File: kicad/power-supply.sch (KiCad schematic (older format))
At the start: 26 parts, among them Q2 2N7002, Q3 MMBT3904, Q4 MMBT3904, Q5 ZXMP10A13FTA, SW6 Ein/Aus, X4 GND-Öse

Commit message: BOM aktualisiert, Zenerdiode: Pinout IPC-konform gestaltet, ...
siehe https://gitlab.com/kicad/libraries/kicad-symbols/-/issues/3157
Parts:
- C22: Index (none) -> 37
- C23: Index (none) -> 44
- C24: Index (none) -> 7
- D8: Index (none) -> 32
- D9: footprint Diode_SMD:D_SOT-23_ANK -> Package_TO_SOT_SMD:SOT-23; symbol Diode:BZX84Cxx -> htl_semiconductors:BZX84Cxx; Index (none) -> 3
- F1, Item3: Index (none) -> 23
- Item4: Index (none) -> 18
- Q2: Index (none) -> 20
- Q3, Q4: Index (none) -> 36
- Q5: Index (none) -> 8
- R32, R33, R34, R37: Index (none) -> 15
- R35: Index (none) -> 26
- R36, R38, R40: Index (none) -> 12
- R39: DistOrderNr (none) -> R3216-22k; Distributor LCSC -> AufLager; Index (none) -> 57
- R41, R42, R43: Index (none) -> 4
- SW6: Index (none) -> 33
- X4: DistOrderNr (none) -> C238129; Distributor (none) -> LCSC; Index (none) -> 27
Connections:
- net GNDPWR: now also D9.1 (A); no longer D9.2 (A)
- net at Q2.1 (G), Q3.1 (B), R33.1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: now also D9.3 (K); no longer D9.1 (K)
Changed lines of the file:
@@
 F 10 "500" H 2700 3650 50  0001 C CNN "PriceForQty"
 F 11 "https://lcsc.com/product-detail/Tactile-Switches_XKB-Connectivity-TS-1187A-B-A-B_C318884.html" H 2700 3650 50  0001 C CNN "Weblink"
+F 12 "33" H 2700 3650 50  0001 C CNN "Index"
 	1    2700 3650
 	0    -1   -1   0
@@
 F 6 "LCSC" H 2700 4550 50  0001 C CNN "Distributor"
 F 7 "10kΩ ±5% 0.25W ±100ppm/℃ 3216 Chip Resistor" H 2700 4550 50  0001 C CNN "Notes"
+F 8 "15" H 2700 4550 50  0001 C CNN "Index"
 	1    2700 4550
 	1    0    0    -1
@@
 F 6 "LCSC" H 2350 5200 50  0001 C CNN "Distributor"
 F 7 "10kΩ ±5% 0.25W ±100ppm/℃ 3216 Chip Resistor" H 2350 5200 50  0001 C CNN "Notes"
+F 8 "15" H 2350 5200 50  0001 C CNN "Index"
 	1    2350 5200
 	1    0    0    -1
 $EndComp
 $Comp
-L Diode:BZX84Cxx D9
+L htl_semiconductors:BZX84Cxx D9
 U 1 1 60911C30
 P 2700 5200
 F 0 "D9" V 2654 5279 50  0000 L CNN
 F 1 "4V7" V 2745 5279 50  0000 L CNN
-F 2 "Diode_SMD:D_SOT-23_ANK" H 2700 5025 50  0001 C CNN
+F 2 "Package_TO_SOT_SMD:SOT-23" H 2700 5025 50  0001 C CNN
 F 3 "https://diotec.com/tl_files/diotec/files/pdf/datasheets/bzx84c2v4.pdf" H 2700 5200 50  0001 C CNN
 F 4 "C12727" H 2700 5200 50  0001 C CNN "DistOrderNr"
@@
 F 7 "0.014" H 2700 5200 50  0001 C CNN "PriceEUR"
 F 8 "50" H 2700 5200 50  0001 C CNN "PriceForQty"
+F 9 "3" H 2700 5200 50  0001 C CNN "Index"
 	1    2700 5200
 	0    1    1    0
@@
 F 7 "50" H 3300 4850 50  0001 C CNN "PriceForQty"
 F 8 "https://lcsc.com/product-detail/Transistors-NPN-PNP_KEXIN-MMBT3904_C382281.html" H 3300 4850 50  0001 C CNN "Weblink"
+F 9 "36" H 3300 4850 50  0001 C CNN "Index"
 	1    3300 4850
 	1    0    0    -1
@@
 F 7 "50" H 4050 4850 50  0001 C CNN "PriceForQty"
 F 8 "https://lcsc.com/product-detail/Transistors-NPN-PNP_KEXIN-MMBT3904_C382281.html" H 4050 4850 50  0001 C CNN "Weblink"
+F 9 "36" H 4050 4850 50  0001 C CNN "Index"
 	1    4050 4850
 	-1   0    0    -1
@@
 F 6 "LCSC" H 3650 3400 50  0001 C CNN "Distributor"
 F 7 "10kΩ ±5% 0.25W ±100ppm/℃ 3216 Chip Resistor" H 3650 3400 50  0001 C CNN "Notes"
+F 8 "15" H 3650 3400 50  0001 C CNN "Index"
 	1    3650 3400
 	1    0    0    -1
@@
 F 5 "C229599" H 3250 5400 50  0001 C CNN "DistOrderNr"
 F 6 "LCSC" H 3250 5400 50  0001 C CNN "Distributor"
+F 7 "26" H 3250 5400 50  0001 C CNN "Index"
 	1    3250 5400
 	1    0    0    -1
@@
 F 9 "0.0106" H 4050 3400 50  0001 C CNN "PriceEUR"
 F 10 "500" H 4050 3400 50  0001 C CNN "PriceForQty"
+F 11 "44" H 4050 3400 50  0001 C CNN "Index"
 	1    4050 3400
 	1    0    0    -1
@@
 F 9 "1kΩ ±5% 0.25W ±100ppm/℃ 1206 Chip Resistor" H 4500 5300 50  0001 C CNN "Notes"
 F 10 "50" H 4500 5300 50  0001 C CNN "PriceForQty"
+F 11 "12" H 4500 5300 50  0001 C CNN "Index"
 	1    4500 5300
 	1    0    0    -1
@@
 F 10 "200" H 1700 1500 50  0001 C CNN "PriceForQty"
 F 11 "https://lcsc.com/product-detail/Fuse-Holders_Shenzhen-lanson-Elec-LS-502_C182320.html" H 1700 1500 50  0001 C CNN "Weblink"
+F 12 "23" H 1700 1500 50  0001 C CNN "Index"
 	1    1700 1500
 	0    1    1    0
@@
 F 8 "https://lcsc.com/product-detail/TVS_Brightking-Elec-TAIWAN-SMCJ48A_C310056.html" H 2000 1700 50  0001 C CNN "Weblink"
 F 9 "TVS-Diode, 1500W, 77.4V, 19.4A" H 2000 1700 50  0001 C CNN "Notes"
+F 10 "32" H 2000 1700 50  0001 C CNN "Index"
 	1    2000 1700
 	0    1    1    0
@@
 F 10 "100" H 1700 1150 50  0001 C CNN "PriceForQty"
 F 11 "https://lcsc.com/product-detail/Cartridge-Fuses_Littelfuse-0618010-MXP_C142673.html" H 1700 1150 50  0001 C CNN "Weblink"
+F 12 "18" H 1700 1150 50  0001 C CNN "Index"
 	1    1700 1150
 	-1   0    0    1
@@
 F 9 "0.2191" H 5000 3700 50  0001 C CNN "PriceEUR"
 F 10 "100" H 5000 3700 50  0001 C CNN "PriceForQty"
+F 11 "8" H 5000 3700 50  0001 C CNN "Index"
 	1    5000 3700
 	1    0    0    1
@@
 F 10 "50" H 1800 5250 50  0001 C CNN "PriceForQty"
 F 11 "https://lcsc.com/product-detail/MOSFET_Guangdong-Hottech-2N7002_C181082.html" H 1800 5250 50  0001 C CNN "Weblink"
+F 12 "20" H 1800 5250 50  0001 C CNN "Index"
 	1    1800 5250
 	-1   0    0    -1
@@
 F 5 "C17928" H 7550 4500 50  0001 C CNN "DistOrderNr"
 F 6 "LCSC" H 7550 4500 50  0001 C CNN "Distributor"
+F 7 "4" H 7550 4500 50  0001 C CNN "Index"
 	1    7550 4500
 	0    1    1    0
@@
 F 5 "C17928" H 9550 4500 50  0001 C CNN "DistOrderNr"
 F 6 "LCSC" H 9550 4500 50  0001 C CNN "Distributor"
+F 7 "4" H 9550 4500 50  0001 C CNN "Index"
 	1    9550 4500
 	0    1    1    0
@@
 F 3 "~" H 5100 5400 50  0001 C CNN
 F 4 "0.01" H 5100 5400 50  0001 C CNN "PriceEUR"
-F 5 "LCSC" H 5100 5400 50  0001 C CNN "Distributor"
+F 5 "AufLager" H 5100 5400 50  0001 C CNN "Distributor"
+F 6 "R3216-22k" H 5100 5400 50  0001 C CNN "DistOrderNr"
+F 7 "57" H 5100 5400 50  0001 C CNN "Index"
 	1    5100 5400
 	1    0    0    -1
@@
 F 9 "1kΩ ±5% 0.25W ±100ppm/℃ 1206 Chip Resistor" H 5100 5850 50  0001 C CNN "Notes"
 F 10 "50" H 5100 5850 50  0001 C CNN "PriceForQty"
+F 11 "12" H 5100 5850 50  0001 C CNN "Index"
 	1    5100 5850
 	1    0    0    -1
@@
 F 9 "0.0233" H 5600 5950 50  0001 C CNN "PriceEUR"
 F 10 "100" H 5600 5950 50  0001 C CNN "PriceForQty"
+F 11 "7" H 5600 5950 50  0001 C CNN "Index"
 	1    5600 5950
 	1    0    0    -1
@@
 F 6 "LCSC" H 1700 4550 50  0001 C CNN "Distributor"
 F 7 "10kΩ ±5% 0.25W ±100ppm/℃ 3216 Chip Resistor" H 1700 4550 50  0001 C CNN "Notes"
+F 8 "15" H 1700 4550 50  0001 C CNN "Index"
 	1    1700 4550
 	1    0    0    -1
@@
 F 9 "0.0123" H 2850 3400 50  0001 C CNN "PriceEUR"
 F 10 "50" H 2850 3400 50  0001 C CNN "PriceForQty"
+F 11 "37" H 2850 3400 50  0001 C CNN "Index"
 	1    2850 3400
 	0    -1   -1   0
@@
 F 5 "C17928" H 5450 4500 50  0001 C CNN "DistOrderNr"
 F 6 "LCSC" H 5450 4500 50  0001 C CNN "Distributor"
+F 7 "4" H 5450 4500 50  0001 C CNN "Index"
 	1    5450 4500
 	0    1    1    0
@@
 F 10 "200" H 1700 800 50  0001 C CNN "PriceForQty"
 F 11 "https://lcsc.com/product-detail/Fuse-Holders_Shenzhen-lanson-Elec-LS-502_C182320.html" H 1700 800 50  0001 C CNN "Weblink"
+F 12 "23" H 1700 800 50  0001 C CNN "Index"
 	1    1700 800
 	1    0    0    -1
@@
 F 9 "1kΩ ±5% 0.25W ±100ppm/℃ 1206 Chip Resistor" H 3550 5400 50  0001 C CNN "Notes"
 F 10 "50" H 3550 5400 50  0001 C CNN "PriceForQty"
+F 11 "12" H 3550 5400 50  0001 C CNN "Index"
 	1    3550 5400
 	1    0    0    -1
@@
 F 2 "htl_smd:Keystone_5016" H 6650 6050 50  0001 C CNN
 F 3 "~" H 6650 6050 50  0001 C CNN
+F 4 "C238129" H 6650 6050 50  0001 C CNN "DistOrderNr"
+F 5 "LCSC" H 6650 6050 50  0001 C CNN "Distributor"
+F 6 "27" H 6650 6050 50  0001 C CNN "Index"
 	1    6650 6050
 	1    0    0    -1

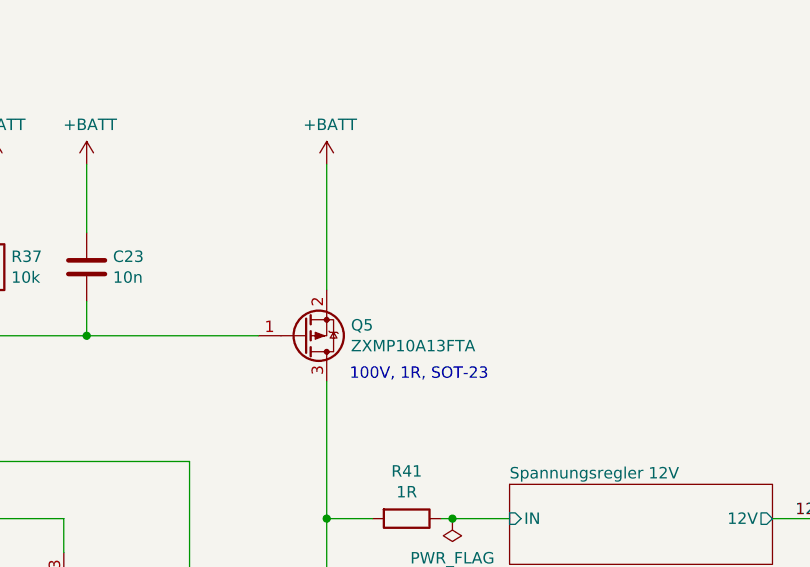
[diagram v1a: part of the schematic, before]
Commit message: MOSFET Alternative
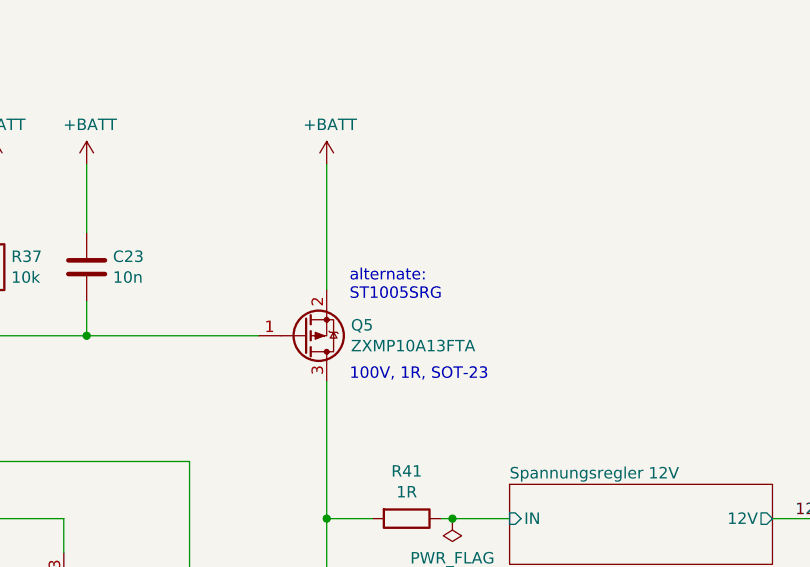
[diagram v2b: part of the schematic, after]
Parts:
- Q5: NotesAlt (none) -> https://lcsc.com/product-detail/MOSFETs_STANSON-Tech-ST1005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
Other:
- note added: "alternate: \nST1005SRG"
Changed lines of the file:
@@
 F 10 "100" H 5000 3700 50  0001 C CNN "PriceForQty"
 F 11 "8" H 5000 3700 50  0001 C CNN "Index"
+F 12 "https://lcsc.com/product-detail/MOSFETs_STANSON-Tech-ST1005SRG_C2682898.html" H 5000 3700 50  0001 C CNN "NotesAlt"
 	1    5000 3700
 	1    0    0    1
@@
 Text Label 7150 4500 0    50   ~ 0
 12Va
+Text Notes 5200 3550 0    50   ~ 0
+alternate: \nST1005SRG
 $EndSCHEMATC

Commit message: Kleine Anpassungen in KiCad-SCH und Firmware
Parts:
- D9: symbol htl_semiconductors:BZX84Cxx -> jbc-miniregler-rescue:BZX84Cxx-htl_semiconductors
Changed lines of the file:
@@
 $EndComp
 $Comp
-L htl_semiconductors:BZX84Cxx D9
+L jbc-miniregler-rescue:BZX84Cxx-htl_semiconductors D9
 U 1 1 60911C30
 P 2700 5200
